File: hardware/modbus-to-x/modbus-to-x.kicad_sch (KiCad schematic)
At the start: 50 parts, among them J1 PWR, J2 UART, SW1 SW_Push, SW2 SW_Push, U1 AMS1117-3.3, U3 MAX3485, U4 ESP32-WROOM-32D, U5 AT24CS64-XHM, U6 AT24CS64-XHM, U7 LMR14020SQDPRTQ1

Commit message: hardware tweaks
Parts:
- removed C22: 0.1uF, Capacitor_SMD:C_1206_3216Metric_Pad1.33x1.80mm_HandSolder, symbol Device:C
- removed L2: MPZ1005S121CT000, MPZ1005S121CT000:IND_1005_TDK-L, symbol MPZ1005S121CT000:MPZ1005S121CT000
- removed SW1, SW2: SW_Push, Button_Switch_SMD:SW_SPST_Omron_B3FS-105xP, symbol Switch:SW_Push
- removed U4: ESP32-WROOM-32D, RF_Module:ESP32-WROOM-32D, symbol RF_Module:ESP32-WROOM-32D
- added C22: 1uF, CAP_UMA_3X5_NCH, symbol Nichicon 1uF Radial THT UMA1H010MCD2TP:UMA1H010MCD2TP
- added C24: 22uF, Capacitor_SMD:C_0805_2012Metric_Pad1.18x1.45mm_HandSolder, symbol Device:C
- added C25: 0.1uF, Capacitor_SMD:C_1206_3216Metric_Pad1.33x1.80mm_HandSolder, symbol Device:C
- added J3: Screw_Terminal_3.5mm_2, SparkFun-Connector:Screw_Terminal_3.5mm-2, symbol SparkFun-Connector:Screw_Terminal_3.5mm_2
- added R14, R2: 620R, Resistor_SMD:R_0805_2012Metric_Pad1.20x1.40mm_HandSolder, symbol Device:R
- added R15: 10K, Resistor_SMD:R_0805_2012Metric_Pad1.20x1.40mm_HandSolder, symbol Device:R
- added SW1, SW2: 1825910-7, digikey-footprints:Switch_Tactile_SMD_6x6mm_PTS645, symbol dk_Tactile-Switches:1825910-7
- added U2: ESP32-WROOM-32DM113DH6400PH3Q0, ESP32-WROOM-32D-M113DH6400PH3Q0:ESP32-WROOM-32DM113DH6400PH3Q0_EXP, symbol ESP32-WROOM-32D-M113DH6400PH3Q0:ESP32-WROOM-32DM113DH6400PH3Q0
- C6: value 22uF -> 0.1uF; footprint Capacitor_SMD:C_0805_2012Metric_Pad1.18x1.45mm_HandSolder -> Capacitor_SMD:C_1206_3216Metric_Pad1.33x1.80mm_HandSolder; PartNo CL21A226MOCLRNC -> CVNF100K12X; Voltage 16V -> 50V
- R1: value 100R -> 120R
- U7: footprint LMR14020SQDPRTQ1:DPR0010A -> LMR14020SQDPRTQ1:DPR0010A_3mm_thermals
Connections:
- net RS485_RE is gone; now on net RS485_DE_RE: U3.2 (~{RE})
- net EN: now also SW2.4, U2.3 (EN)
- net GND: now also C7.2, U7.V (GND_STITCH), C22.2, C24.1, C25.1, R14.1, SW1.2, SW2.2, U2.1 (GND), U2.15 (GND), U2.38 (GND), U2.39 (GND), U2.V (GND_STITCH); no longer C5.2, C6.1, C7.1
- net IO_0: now also SW1.4, U2.25 (IO0); no longer C5.1
- net PGOOD: now also U2.16 (IO13)
- net RX_0: now also U2.34 (RXD0)
- net SCL_BUS: now also U2.36 (IO22)
- net SDA_BUS: now also U2.33 (IO21)
- net TX_0: now also U2.35 (TXD0)
- net VBUS_12: now also D3.1 (A1), J1.1 (Pin_1)
- net VDD33: now also C7.1, C22.1, C24.2, C25.2, R15.1, R2.2, U2.2 (3V3); no longer C6.2, C7.2
- net MB_INT_A renamed RS485+
- net RS485+: now also J3.1 (Pin_1), R2.1
- net MB_INT_B renamed RS485-
- net RS485-: now also J3.2 (Pin_2), R14.2
- net RS485_DE renamed RS485_DE_RE
- net RS485_DE_RE: now also R15.2, U2.23 (IO15)
- net RX_2 renamed RX_{2}
- net RX_{2}: now also U2.27 (IO16)
- net TX_2 renamed TX_{2}
- net TX_{2}: now also U2.28 (IO17)
- new net: C5.2, SW1.1
- new net: C5.1, SW1.3
- new net: C6.1, SW2.3
- new net: C6.2, SW2.1
- no-connect marks 28 -> 30
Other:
- note added: "RS485 DE/RE Pull-Up"
- moved on the sheet: D1, D3, J1, J2, R1, R3, U3

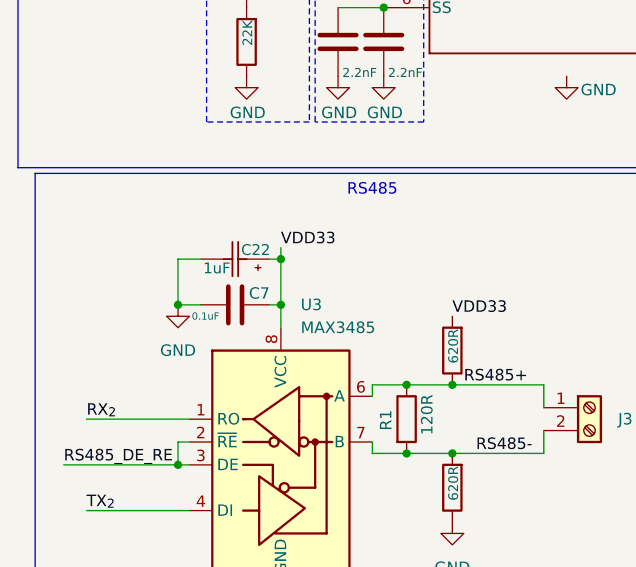
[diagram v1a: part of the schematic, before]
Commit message: added bulk ecap to max485 ic
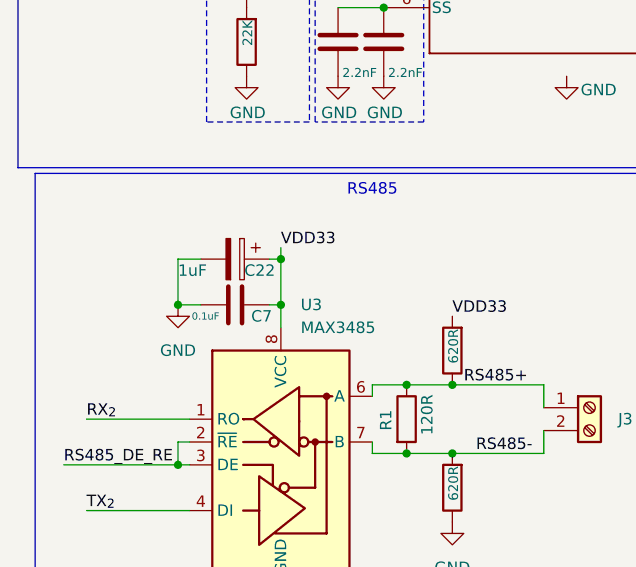
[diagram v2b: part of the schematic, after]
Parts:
- removed C22: 1uF, CAP_UMA_3X5_NCH, symbol Nichicon 1uF Radial THT UMA1H010MCD2TP:UMA1H010MCD2TP
- added C22: 1uF, Capacitor_SMD:CP_Elec_4x5.4, symbol Device:C_Polarized
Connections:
- net GND: now also C22.2
- net VDD33: now also C22.1
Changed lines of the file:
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@@
 		(dnp no)
 		(property "Reference" "C7"
-			(at 38.354 85.09 90)
+			(at 38.608 87.63 90)
 			(effects
 				(font
@@
 	)
 	(symbol
-		(lib_id "Nichicon 1uF Radial THT UMA1H010MCD2TP:UMA1H010MCD2TP")
-		(at 40.64 81.28 180)
-		(unit 1)
-		(exclude_from_sim no)
-		(in_bom yes)
-		(on_board yes)
-		(dnp no)
-		(property "Reference" "C22"
-			(at 39.116 80.264 0)
-			(effects
-				(font
-					(size 1.2 1.2)
-				)
-			)
-		)
-		(property "Value" "1uF"
-			(at 34.798 82.296 0)
-			(effects
-				(font
-					(size 1.2 1.2)
-				)
-			)
-		)
-		(property "Footprint" "CAP_UMA_3X5_NCH"
-			(at 40.64 81.28 0)
-			(effects
-				(font
-					(size 1.27 1.27)
-					(italic yes)
-				)
-				(hide yes)
-			)
-		)
-		(property "Datasheet" "https://www.nichicon.co.jp/english/products/pdf/e-mi_tape.pdf"
-			(at 40.64 81.28 0)
-			(effects
-				(font
-					(size 1.27 1.27)
-					(italic yes)
-				)
-				(hide yes)
-			)
-		)
-		(property "Description" "1 µF 50 V Aluminum Electrolytic Capacitors Radial, Can 2000 Hrs @ 85°C"
-			(at 40.64 81.28 0)
-			(effects
-				(font
-					(size 1.27 1.27)
-				)
-				(hide yes)
-			)
-		)
-		(property "PartNo" "UMA1H010MCD2TP"
-			(at 40.64 81.28 0)
-			(effects
-				(font
-					(size 1.27 1.27)
-				)
-				(hide yes)
-			)
-		)
-		(pin "1"
-		)
-		(pin "2"
-		)
-		(instances
-			(project ""
-				(path "/d5b026e9-d5a5-415b-84cb-4c68355c0f8f"
-					(reference "C22")
-					(unit 1)
-				)
-			)
-		)
-	)
-	(symbol
 		(lib_id "power:GND")
 		(at 195.58 106.68 0)
@@
 					(unit 1)
 				)
+			)
+		)
+	)
+	(symbol
+		(lib_id "Device:C_Polarized")
+		(at 36.83 81.28 270)
+		(unit 1)
+		(exclude_from_sim no)
+		(in_bom yes)
+		(on_board yes)
+		(dnp no)
+		(property "Reference" "C22"
+			(at 37.846 82.55 90)
+			(effects
+				(font
+					(size 1.27 1.27)
+				)
+				(justify left)
+			)
+		)
+		(property "Value" "1uF"
+			(at 30.48 82.55 90)
+			(effects
+				(font
+					(size 1.27 1.27)
+				)
+				(justify left)
+			)
+		)
+		(property "Footprint" "Capacitor_SMD:CP_Elec_4x5.4"
+			(at 33.02 82.2452 0)
+			(effects
+				(font
+					(size 1.27 1.27)
+				)
+				(hide yes)
+			)
+		)
+		(property "Datasheet" "https://elektronik-lavpris.dk/files/sup2/KJ-HT.pdf"
+			(at 36.83 81.28 0)
+			(effects
+				(font
+					(size 1.27 1.27)
+				)
+				(hide yes)
+			)
+		)
+		(property "Description" "SMD El-Capacitor 1uF/50V 4x5,4mm"
+			(at 36.83 81.28 0)
+			(effects
+				(font
+					(size 1.27 1.27)
+				)
+				(hide yes)
+			)
+		)
+		(property "Voltage" "50V"
+			(at 32.004 83.312 0)
+			(effects
+				(font
+					(size 1.27 1.27)
+				)
+				(hide yes)
+			)
+		)
+		(property "PartNo" "CHS0001/50"
+			(at 36.83 81.28 0)
+			(effects
+				(font
+					(size 1.27 1.27)
+				)
+				(hide yes)
+			)
+		)
+		(property "FriendlyName" "Cout47uf"
+			(at 36.83 81.28 0)
+			(effects
+				(font
+					(size 1.27 1.27)
+				)
+				(hide yes)
+			)
+		)
+		(property "ProductCode" ""
+			(at 36.83 81.28 0)
+			(effects
+				(font
+					(size 1.27 1.27)
+				)
+				(hide yes)
+			)
+		)
+		(pin "2"
+		)
+		(pin "1"
+		)
+		(instances
+			(project "modbus-to-x"
+				(path "/d5b026e9-d5a5-415b-84cb-4c68355c0f8f"
+					(reference "C22")
+					(unit 1)
+				)

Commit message: status leds
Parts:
- added D4, D5, D6: LED, LED_SMD:LED_0402_1005Metric_Pad0.77x0.64mm_HandSolder, symbol Device:LED
- added R16, R17, R18: 2K, Resistor_SMD:R_0603_1608Metric_Pad0.98x0.95mm_HandSolder, symbol Device:R
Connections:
- net GND: now also D4.1 (K), D5.1 (K), D6.1 (K)
- net STAT_2: now reaches U2.10 (IO25)
- net STAT_2: now also R17.1
- net STAT_3: now reaches U2.11 (IO26)
- net STAT_3: now also R18.1
- net STAT_1: now reaches U2.9 (IO33)
- net STAT_1: now also R16.1
- new net: D4.2 (A), R16.2
- new net: D5.2 (A), R17.2
- new net: D6.2 (A), R18.2
- no-connect marks 30 -> 27
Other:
- note added: "Status LEDs"

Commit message: board cleanup
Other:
- company: (none) -> Joachim Andersen
- title: (none) -> Modbus-to-X
- moved on the sheet: C1, C12, C13, C14, C15, C16, C17, C18, C19, C2, C21, D2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

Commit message: added receptable
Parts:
- added J4: SSQ-110-X-X-D, Connector Receptable 2x10 20POS:SAMTEC_SSQ-110-X-X-D, symbol Connector Receptable 2x10 20POS:SSQ-110-X-X-D
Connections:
- net GND: now also J4.01, J4.02, J4.11, J4.20
- net RS485_DE_RE: now also J4.04
- net RX_0: now also J4.13
- net RX_{2}: now also J4.07
- net SCL_BUS: now also J4.06
- net SDA_BUS: now also J4.05
- net TX_0: now also J4.14
- net TX_{2}: now also J4.08
- net VBUS_12: now also J4.19
- net VCC5: now also J4.18
- net VDD33: now also J4.09
- no-connect marks 27 -> 33

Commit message: improved edge cuts
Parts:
- added TP_RX2_TX2: TestPoint_2Pole, Connector_PinHeader_2.54mm:PinHeader_1x02_P2.54mm_Vertical, symbol Connector:TestPoint_2Pole
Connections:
- net RS485_DE_RE: now also J4.17; no longer J4.04
- net RX_0: no longer J4.13
- net RX_{2}: now also TP_RX2_TX2.2; no longer J4.07
- net TX_0: no longer J4.14
- net TX_{2}: now also TP_RX2_TX2.1; no longer J4.08
- net SPI_CS: now reaches U2.29 (IO5)
- net SPI_CS: now also J4.12
- net SPI_CLK: now reaches U2.30 (IO18)
- net SPI_CLK: now also J4.14
- net SPI_MISO: now reaches U2.31 (IO19)
- net SPI_MISO: now also J4.13
- net SPI_MOSI: now reaches U2.37 (IO23)
- net SPI_MOSI: now also J4.15
- no-connect marks 33 -> 29
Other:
- moved on the sheet: J4

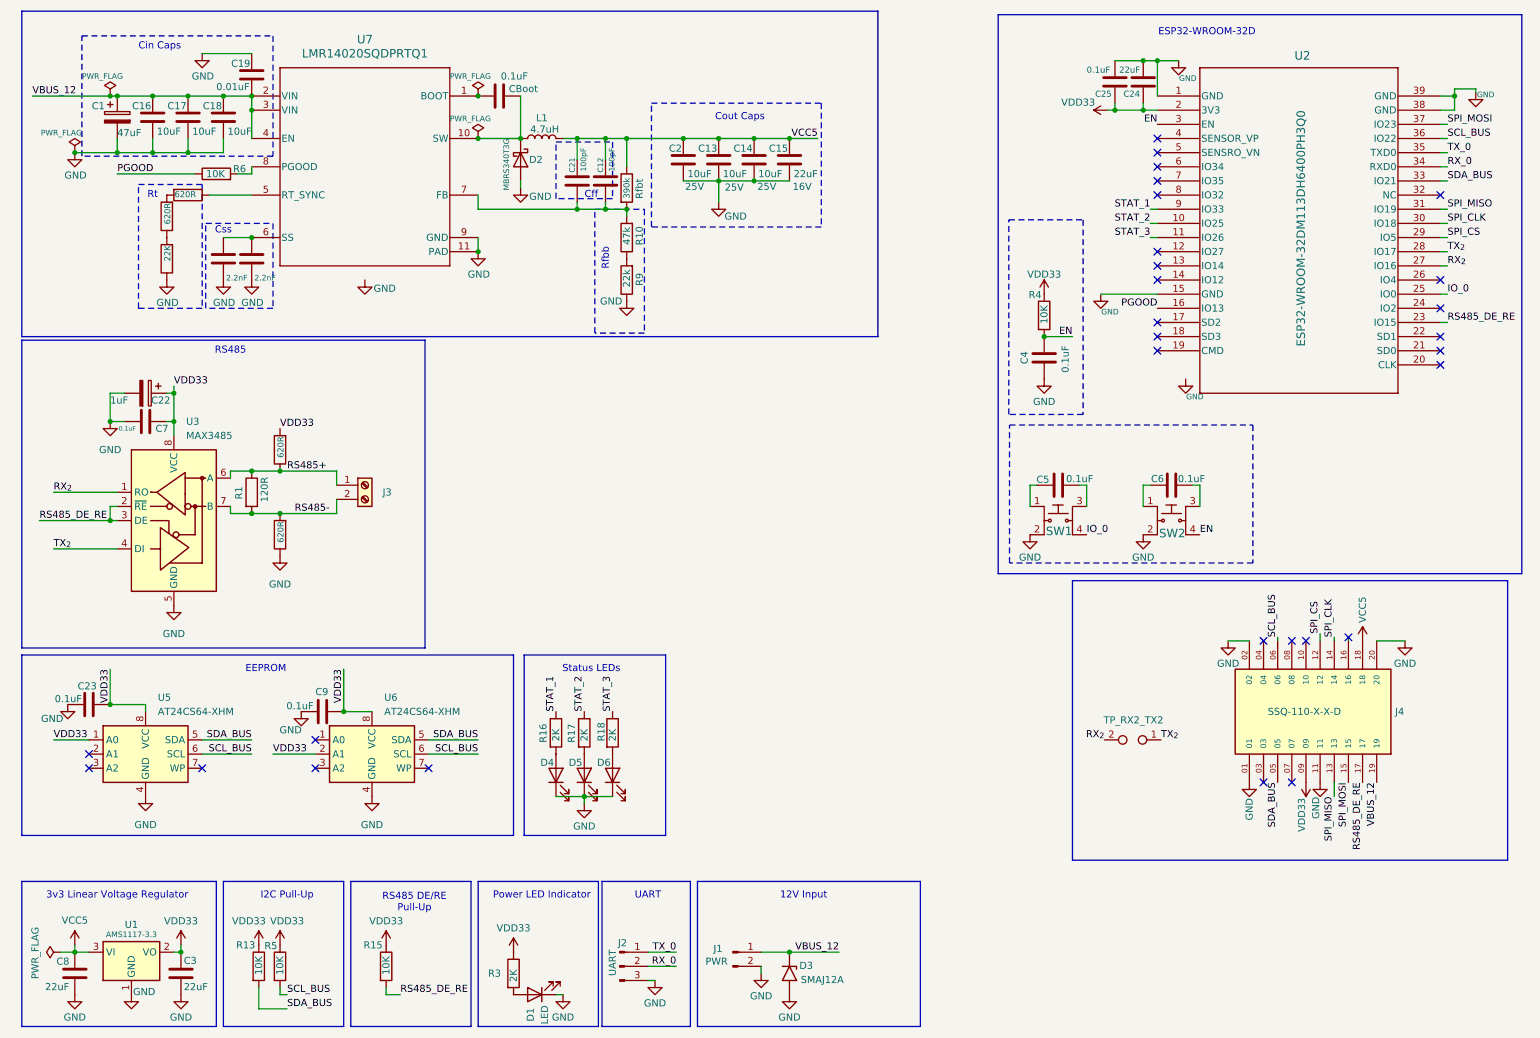
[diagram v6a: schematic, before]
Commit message: improved trace clearance
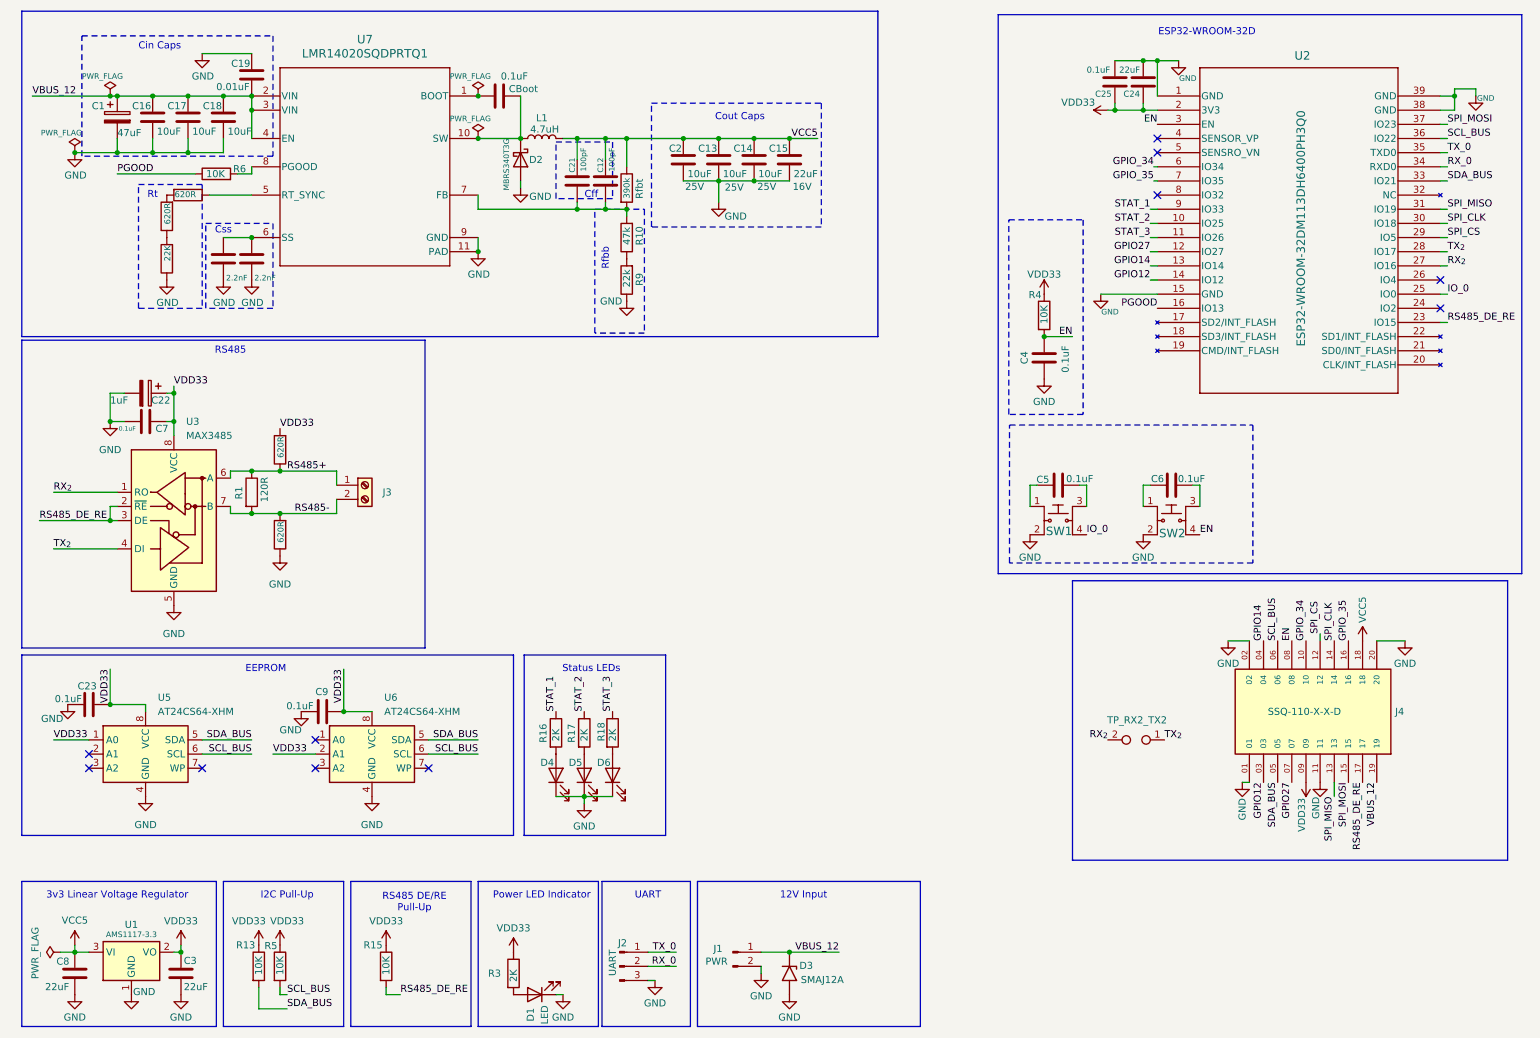
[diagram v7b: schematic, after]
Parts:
- U2: footprint ESP32-WROOM-32D-M113DH6400PH3Q0:ESP32-WROOM-32DM113DH6400PH3Q0_EXP -> ESP32-WROOM-32D-M113DH6400PH3Q0:ESP32-WROOM-32DM113DH6400PH3Q0_WITH_VIAS
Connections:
- net EN: now also J4.08
- net GND: no longer U2.V (GND_STITCH)
- net GPIO27: now reaches U2.12 (IO27)
- net GPIO27: now also J4.07
- net GPIO14: now reaches U2.13 (IO14)
- net GPIO14: now also J4.04
- net GPIO12: now reaches U2.14 (IO12)
- net GPIO12: now also J4.03
- net GPIO_34: now reaches U2.6 (IO34)
- net GPIO_34: now also J4.10
- net GPIO_35: now reaches U2.7 (IO35)
- net GPIO_35: now also J4.16
- no-connect marks 29 -> 11
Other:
- moved on the sheet: TP_RX2_TX2
